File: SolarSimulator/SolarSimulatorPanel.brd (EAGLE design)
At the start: 150 x 70 mm, 82 parts, among them U1 Red Driver, U2 LM3404HVMA, U3 Blue Driver, X1 MKDSN1,5/2-5,08

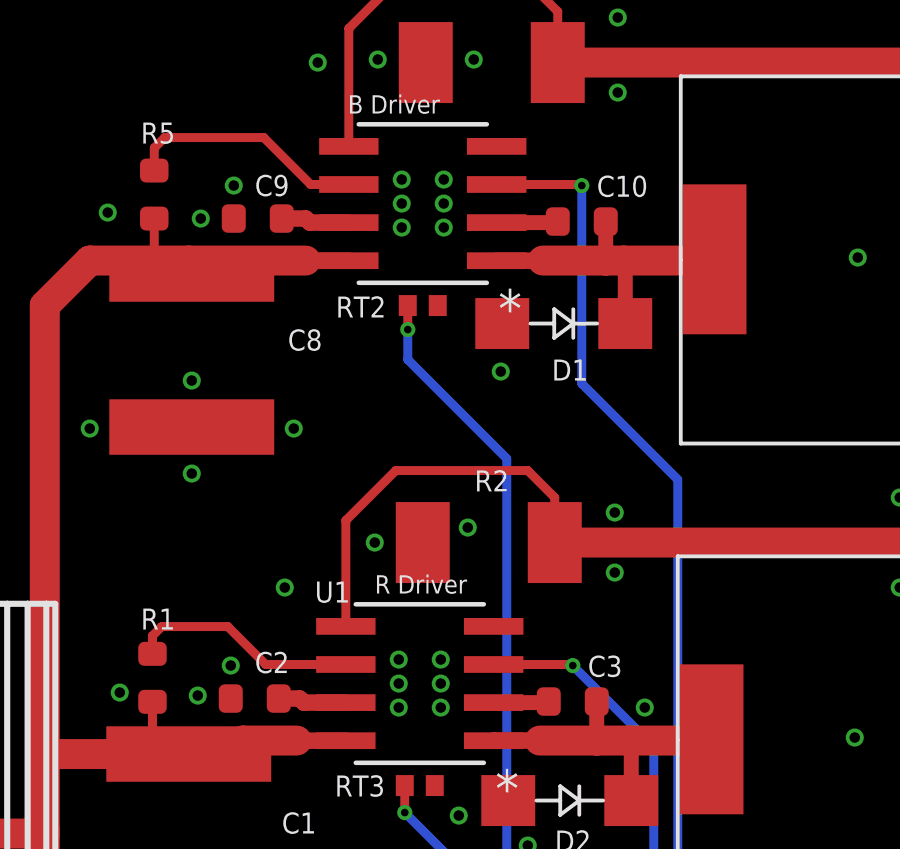
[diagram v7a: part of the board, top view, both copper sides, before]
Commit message: added BOM and cleaned up schematic a bit
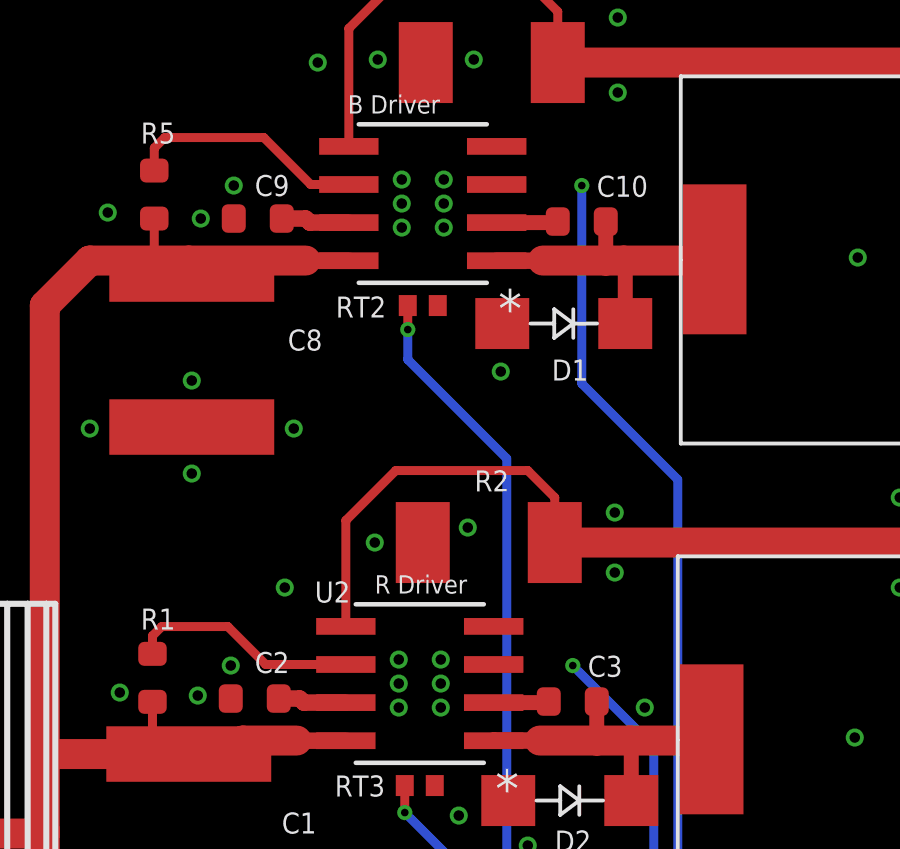
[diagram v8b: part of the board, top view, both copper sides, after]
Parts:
- removed GREEN, GREEN9, RED: X-QE, solarsim:X-QE
- added GREE9, GREEN15, RED15: X-QE, solarsim:X-QE
- C1, C6, C8: value (none) -> 1 uF 120V
- C10, C3, C7: value 10n 25V -> 10nF 25V
- C11, C4, C5: value 10u -> 10uF
- C12, C9: value 100n 25V -> 100nF 25V
- R2, R3, R6: value (none) -> 137 m
- U1: value Red Driver -> Blue Driver
- U2: value LM3404HVMA -> Red Driver
- U3: value Blue Driver -> Green Driver
- moved U3 31.5 mm to (20.4, 28.7)
- moved GREEN1 20.0 mm to (59.0, 44.0)
- moved GREEN11 20.0 mm to (59.0, 20.0)
- moved GREEN12 20.0 mm to (79.0, 20.0)
- moved GREEN13 20.0 mm to (99.0, 20.0)
- moved GREEN14 20.0 mm to (119.0, 20.0)
- moved GREEN2 20.0 mm to (79.0, 44.0)
- moved GREEN3 20.0 mm to (99.0, 44.0)
- moved GREEN4 20.0 mm to (119.0, 44.0)
- moved GREEN6 20.0 mm to (139.0, 32.0)
- moved GREEN7 20.0 mm to (119.0, 32.0)
- moved GREEN8 20.0 mm to (99.0, 32.0)
- moved RED1 20.0 mm to (64.0, 50.0)
- moved RED11 20.0 mm to (64.0, 26.0)
- moved RED12 20.0 mm to (84.0, 26.0)
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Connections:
- removed net N$14 (its old number): RED.CATHODE, RED1.ANODE
- removed net N$2 (its old number): GREEN10.ANODE, GREEN9.CATHODE
- removed net N$35 (its old number): GREEN.CATHODE, GREEN1.ANODE
- removed net N$5 (its old number): RED5.CATHODE, RED6.ANODE
- new net N$13: RED14.CATHODE, RED15.ANODE
- new net N$17: RED4.CATHODE, RED5.ANODE
- new net N$41: GREE9.ANODE, GREEN8.CATHODE
- new net N$46: GREEN14.CATHODE, GREEN15.ANODE
- net 88: now also RED5.CATHODE, RED6.ANODE; no longer RED4.CATHODE, RED5.ANODE
- net BLUE-RTN: now also U1.5; no longer U3.5
- net D10/PWM_R: now also U2.3; no longer U1.3
- net D11/PWM_G: now also U3.3; no longer U2.3
- net D9/PWM_B: now also U1.3; no longer U3.3
- net GREEN-RTN: now also GREEN15.CATHODE, U3.5; no longer GREEN14.CATHODE, U2.5
- net GRN-OUT: now also GREEN1.ANODE; no longer GREEN.ANODE
- net N$1: now also U3.1; no longer U2.1
- net N$18: now also U1.6; no longer U3.6
- net N$19: now also U3.6; no longer U2.6
- net N$22: now also U2.2; no longer U1.2
- net N$25: now also U2.1; no longer U1.1
- net N$32: now also U3.2; no longer U2.2
- net N$33: now also U3.7; no longer U2.7
- net N$34: now also U1.1; no longer U3.1
- net N$4: now also U2.7; no longer U1.7
- net N$42: now also GREE9.CATHODE, GREEN10.ANODE; no longer GREEN8.CATHODE, GREEN9.ANODE
- net N$52: now also U1.2; no longer U3.2
- net N$53: now also U1.7; no longer U3.7
- net N$6: now also U2.6; no longer U1.6
- net RED-OUT: now also RED1.ANODE; no longer RED.ANODE
- net RED-RTN: now also RED15.CATHODE, U2.5; no longer RED14.CATHODE, U1.5
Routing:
- net N$9: track 12.7 -> 0.00 mm
- net N$88: track 0.00 -> 12.7 mm
- net N$77: track 0.00 -> 12.7 mm
- net N$38: track 12.7 -> 0.00 mm
- net N$2 (its old number): track 12.7 -> 0.00 mm, vias 8 -> 0
- net N$2: track 0.00 -> 12.7 mm
- net D9/PWM_B: track 69.7 -> 66.9 mm
- net D10/PWM_R: track 54.3 -> 51.7 mm
- added copper zone on layer 1, net N$13
- added copper zone on layer 16, net N$13
- added copper zone on layer 1, net N$17
- added copper zone on layer 16, net N$17
- added copper zone on layer 1, net N$41
- added copper zone on layer 16, net N$41
- added copper zone on layer 1, net N$46
- added copper zone on layer 16, net N$46
- removed copper zone on layer 1, net N$14 (its old number)
- removed copper zone on layer 16, net N$14 (its old number)
- removed copper zone on layer 1, net N$2 (its old number)
- removed copper zone on layer 16, net N$2 (its old number)
- removed copper zone on layer 1, net N$35 (its old number)
- removed copper zone on layer 16, net N$35 (its old number)
- removed copper zone on layer 1, net N$5 (its old number)
- removed copper zone on layer 16, net N$5 (its old number)
